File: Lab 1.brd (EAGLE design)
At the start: 25.1 x 25.4 mm, 8 parts

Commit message: ripup
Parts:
- moved C1 1.66 mm to (14.5, 19.9), turned to 180 degrees
- moved C2 0.40 mm to (10.7, 19.9), turned to 180 degrees
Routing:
- net +5V: track 38.7 -> 0.00 mm, vias 3 -> 0
- net GND: track 27.4 -> 0.00 mm
- net SCL: track 25.2 -> 0.00 mm, vias 2 -> 0
- net SDA: track 17.6 -> 0.00 mm
- net EN: track 11.6 -> 0.00 mm, vias 1 -> 0
- net IN: track 10.8 -> 0.00 mm, vias 1 -> 0
- net O+: track 7.25 -> 0.00 mm
- net O-: track 7.20 -> 0.00 mm, vias 1 -> 0
- net N$9: track 5.44 -> 0.00 mm, vias 2 -> 0
- net N$8: track 4.56 -> 0.00 mm
- net N$7: track 3.85 -> 0.00 mm

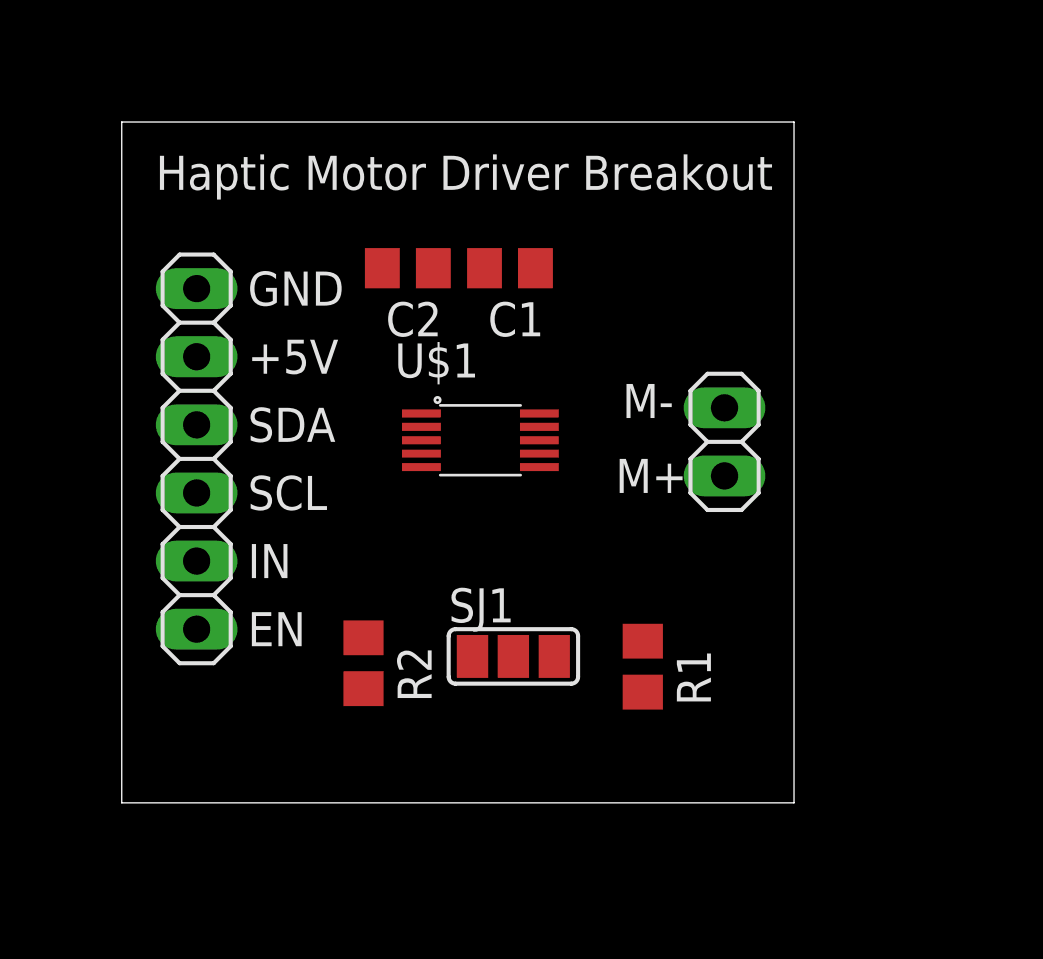
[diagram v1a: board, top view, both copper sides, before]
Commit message: Added Ground Plane. Added Filter Capacitor
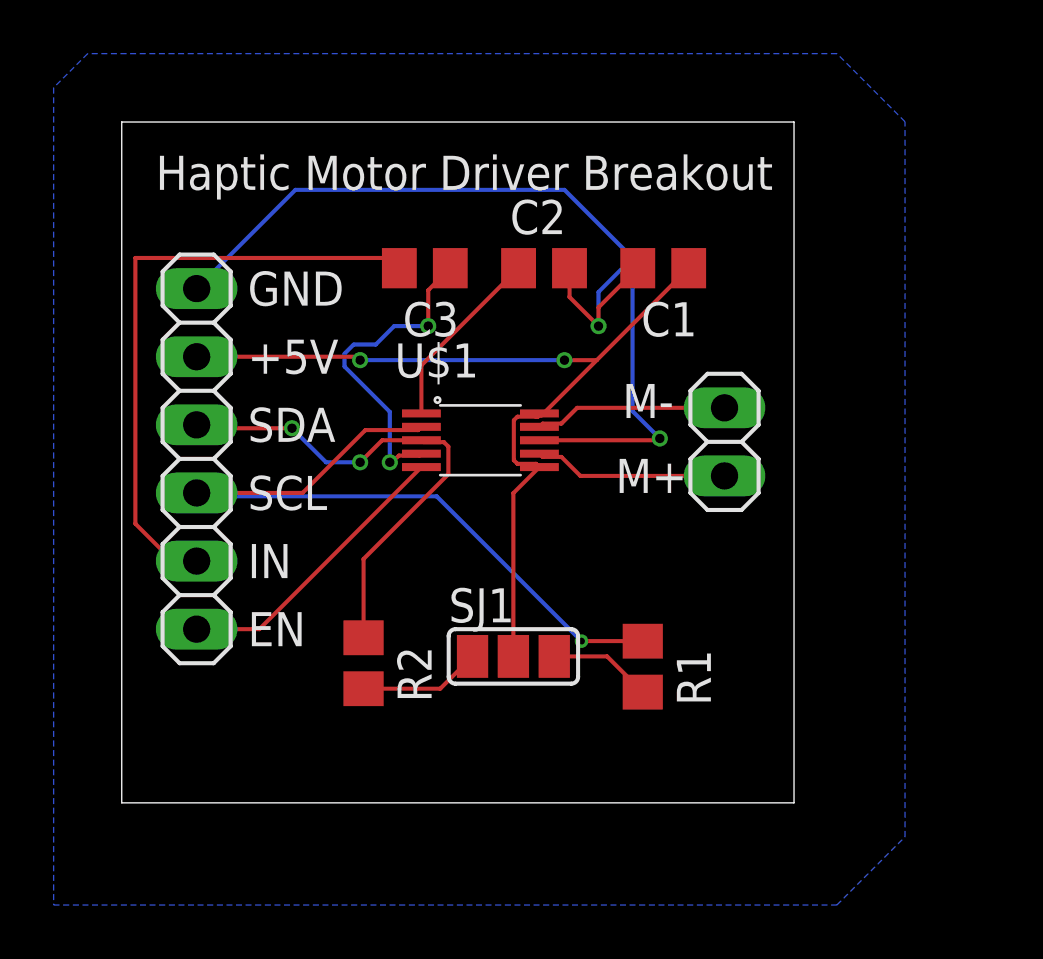
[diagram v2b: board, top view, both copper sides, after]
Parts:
- added C3: (no value), rcl:C0805
- moved C1 5.72 mm to (20.2, 19.9)
- moved C2 5.08 mm to (15.7, 19.9), turned to 0 degrees
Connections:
- new net N$2: C3.1, U$1.P$4
- net IN: now also C3.2; no longer U$1.P$4
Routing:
- net GND: track 0.00 -> 38.9 mm, vias 0 -> 2
- net +5V: track 0.00 -> 34.0 mm, vias 0 -> 2
- net SCL: track 0.00 -> 28.4 mm, vias 0 -> 1
- net IN: track 0.00 -> 22.8 mm
- net SDA: track 0.00 -> 18.8 mm, vias 0 -> 2
- net N$2: track 0.00 -> 12.1 mm, vias 0 -> 2
- net EN: track 0.00 -> 10.9 mm
- net O+: track 0.00 -> 7.25 mm
- net O-: track 0.00 -> 7.20 mm
- net N$9: track 0.00 -> 6.92 mm
- net N$8: track 0.00 -> 4.56 mm
- net N$7: track 0.00 -> 3.85 mm
- added copper zone on layer 16, net N$1

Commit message: Update
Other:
- board size 25.1 x 25.4 mm -> 25.1 x 24.1 mm

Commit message: Updated: Sep 6
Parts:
- moved JP1 3.81 mm to (22.5, 9.65)
- moved JP2 3.81 mm to (2.79, 9.02)
- moved U$1 3.81 mm to (13.1, 9.65)
- moved C1 3.81 mm to (20.2, 16.1)
- moved C2 3.81 mm to (15.7, 16.1)
- moved C3 3.81 mm to (11.3, 16.1)
- moved SJ1 1.57 mm to (15.0, 3.94)
- moved R1 1.57 mm to (19.8, 3.56)
- moved R2 1.57 mm to (9.40, 3.68)
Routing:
- net N$2: track 12.1 -> 14.6 mm
- net SDA: track 18.8 -> 16.4 mm
- net +5V: track 34.0 -> 31.6 mm
- net IN: track 22.8 -> 23.5 mm
- net SCL: track 28.4 -> 27.8 mm
- added copper zone on layer 1, net GND
- added copper zone on layer 16, net GND
- removed copper zone on layer 16, net N$1
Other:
- board size 25.1 x 24.1 mm -> 25.1 x 21.6 mm
- board text added: "Haptic Motor Driver Breakout v1.0"
- board text added: "Ibrahim AlQattan - Giselle Koo"
- board text removed: "Haptic Motor Driver Breakout"

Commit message: Updated: Sep 6
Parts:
- moved C2 0.40 mm to (15.9, 15.7)
- moved C1 0.40 mm to (20.3, 15.7)
- moved C3 0.40 mm to (11.4, 15.7)
- moved JP2 0.40 mm to (2.92, 8.64)
- moved R2 0.40 mm to (9.53, 3.30)
- moved R1 0.40 mm to (19.9, 3.17)
- moved SJ1 0.40 mm to (15.1, 3.56)
- moved JP1 0.40 mm to (22.6, 9.27)
- moved U$1 0.40 mm to (13.2, 9.27)
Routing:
- net GND: track 38.9 -> 37.6 mm
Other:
- board size 25.1 x 21.6 mm -> 24.7 x 17.4 mm
- board text added: "Haptic Motor Driver Breakout | v1.0"
- board text added: "Ibrahim AlQattan Giselle Koo"
- board text removed: "Haptic Motor Driver Breakout v1.0"
- board text removed: "Ibrahim AlQattan - Giselle Koo"
